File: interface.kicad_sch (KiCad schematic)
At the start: 59 parts, among them J5 5034801200, SW1 TS35CA, U10 LIS2DW12TR, U11 AP3602AKTR-G1, U8 DRV2603RUNT, U9 TPS61040DBV

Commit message: fixups before manufacturing pt1
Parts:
- removed U10: LIS2DW12TR, LIS2DW12TR:LGA-12_L2.0-W2.0-P0.50-BL, symbol LIS2DW12TR:LIS2DW12TR
- added U10: LIS3DH, Package_LGA:LGA-16_3x3mm_P0.5mm_LayoutBorder3x5y, symbol Sensor_Motion:LIS3DH
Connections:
- net ACC_3V3_IN: now also U10.1 (VDD_IO), U10.14 (VDD), U10.8 (CS)
- net GND: now also U10.10 (GND), U10.12 (GND), U10.5 (GND)
- net at JP17.1 (A): now also U10.11 (INT1)
- net at JP15.2 (B): now also U10.4 (SPC)
- net at JP14.2 (B): now also U10.6 (SDI)
- no-connect marks 8 -> 9
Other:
- moved on the sheet: C33, C34, C35, JP14, JP15, JP16, JP17

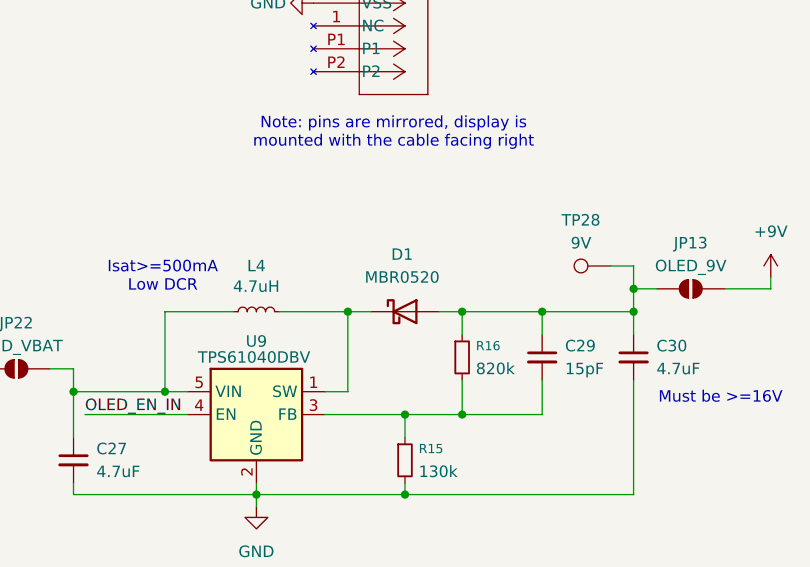
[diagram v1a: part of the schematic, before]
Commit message: oops fix: reversed diodes
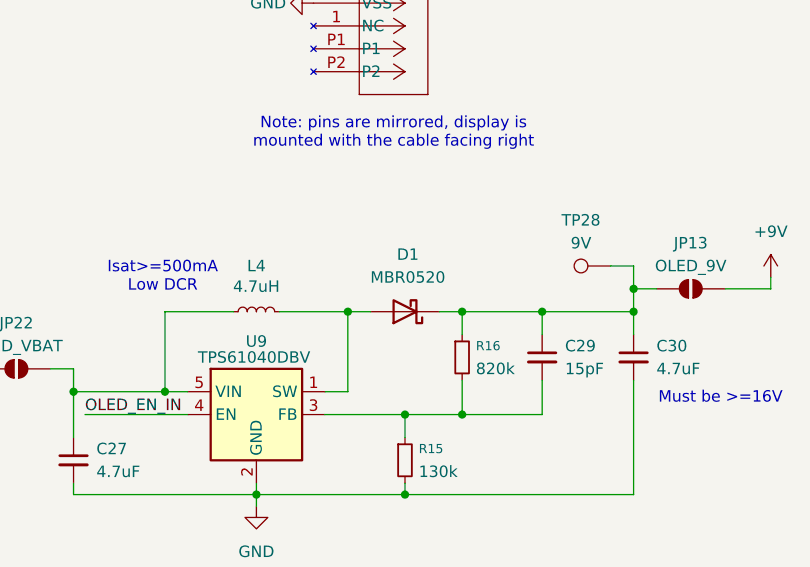
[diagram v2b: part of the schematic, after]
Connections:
- net at C29.1, C30.1, JP13.1 (A)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: now also D1.1 (K); no longer D1.2 (A)
- net at L4.2, U9.1 (SW): now also D1.2 (A); no longer D1.1 (K)
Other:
- moved on the sheet: D1
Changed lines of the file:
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@@
 	(symbol
 		(lib_id "Diode:MBR0520")
-		(at 133.35 143.51 0)
+		(at 133.35 143.51 180)
 		(unit 1)
 		(exclude_from_sim no)
@@
 		(fields_autoplaced yes)
 		(property "Reference" "D1"
-			(at 133.0325 137.16 0)
+			(at 133.6675 137.16 0)
 			(effects
 				(font
@@
 		)
 		(property "Value" "MBR0520"
-			(at 133.0325 139.7 0)
+			(at 133.6675 139.7 0)
 			(effects
 				(font
@@
 		)
 		(property "Footprint" "Diode_SMD:D_SOD-123"
-			(at 133.35 147.955 0)
+			(at 133.35 139.065 0)
 			(effects
 				(font

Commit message: oops fix: accelerometer
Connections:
- net GND: now also U10.7 (SDO)
- net at JP15.2 (B): now also U10.6 (SDI); no longer U10.4 (SPC)
- net at JP14.2 (B): now also U10.4 (SPC); no longer U10.6 (SDI)
- no-connect marks 9 -> 8
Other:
- moved on the sheet: JP14, JP15
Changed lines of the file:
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@@
 	)
 	(no_connect
-		(at 226.06 50.8)
-	)
-	(no_connect
 		(at 59.69 48.26)
 	)
@@
 	(global_label "SCL"
 		(shape input)
-		(at 194.31 48.26 180)
+		(at 194.31 55.88 180)
 		(fields_autoplaced yes)
 		(effects
@@
 		)
 		(property "Intersheetrefs" "${INTERSHEET_REFS}"
-			(at 187.8172 48.26 0)
+			(at 187.8172 55.88 0)
 			(effects
 				(font
@@
 	(global_label "SDA"
 		(shape input)
-		(at 194.31 55.88 180)
+		(at 194.31 48.26 180)
 		(fields_autoplaced yes)
 		(effects
@@
 		)
 		(property "Intersheetrefs" "${INTERSHEET_REFS}"
-			(at 187.7567 55.88 0)
+			(at 187.7567 48.26 0)
 			(effects
 				(font
@@
 	(symbol
 		(lib_id "Jumper:SolderJumper_2_Open")
-		(at 200.66 55.88 0)
+		(at 200.66 48.26 0)
 		(unit 1)
 		(exclude_from_sim no)
@@
 		(dnp no)
 		(property "Reference" "JP15"
-			(at 200.66 50.8 0)
+			(at 200.66 43.18 0)
 			(effects
 				(font
@@
 		)
 		(property "Value" "ACC_SDA"
-			(at 200.66 53.34 0)
+			(at 200.66 45.72 0)
 			(effects
 				(font
@@
 		)
 		(property "Footprint" "Jumper:SolderJumper-2_P1.3mm_Open_Pad1.0x1.5mm"
-			(at 200.66 55.88 0)
+			(at 200.66 48.26 0)
 			(effects
 				(font
@@
 		)
 		(property "Datasheet" "~"
-			(at 200.66 55.88 0)
+			(at 200.66 48.26 0)
 			(effects
 				(font
@@
 		)
 		(property "Description" "Solder Jumper, 2-pole, open"
-			(at 200.66 55.88 0)
+			(at 200.66 48.26 0)
 			(effects
 				(font
@@
 	)
 	(symbol
+		(lib_id "power:GND")
+		(at 226.06 50.8 270)
+		(unit 1)
+		(exclude_from_sim no)
+		(in_bom yes)
+		(on_board yes)
+		(dnp no)
+		(property "Reference" "#PWR013"
+			(at 219.71 50.8 0)
+			(effects
+				(font
+					(size 1.27 1.27)
+				)
+				(hide yes)
+			)
+		)
+		(property "Value" "GND"
+			(at 223.012 50.8 90)
+			(effects
+				(font
+					(size 1.27 1.27)
+				)
+				(justify right)
+			)
+		)
+		(property "Footprint" ""
+			(at 226.06 50.8 0)
+			(effects
+				(font
+					(size 1.27 1.27)
+				)
+				(hide yes)
+			)
+		)
+		(property "Datasheet" ""
+			(at 226.06 50.8 0)
+			(effects
+				(font
+					(size 1.27 1.27)
+				)
+				(hide yes)
+			)
+		)
+		(property "Description" "Power symbol creates a global label with name \"GND\" , ground"
+			(at 226.06 50.8 0)
+			(effects
+				(font
+					(size 1.27 1.27)
+				)
+				(hide yes)
+			)
+		)
+		(pin "1"
+		)
+		(instances
+			(project ""
+				(path "/c6cb5a1d-9f97-4766-8582-a9e93ed049e4/24c06676-89c1-498c-8350-9d02668ef39e"
+					(reference "#PWR013")
+					(unit 1)
+				)
+			)
+		)
+	)
+	(symbol
 		(lib_id "Device:C_Small")
 		(at 106.68 86.36 90)
@@
 	(symbol
 		(lib_id "Jumper:SolderJumper_2_Open")
-		(at 200.66 48.26 0)
+		(at 200.66 55.88 0)
 		(unit 1)
 		(exclude_from_sim no)
@@
 		(dnp no)
 		(property "Reference" "JP14"
-			(at 200.66 43.18 0)
+			(at 200.66 50.8 0)
 			(effects
 				(font
@@
 		)
 		(property "Value" "ACC_SCL"
-			(at 200.66 45.72 0)
+			(at 200.66 53.34 0)
 			(effects
 				(font
@@
 		)
 		(property "Footprint" "Jumper:SolderJumper-2_P1.3mm_Open_Pad1.0x1.5mm"
-			(at 200.66 48.26 0)
+			(at 200.66 55.88 0)
 			(effects
 				(font
@@
 		)
 		(property "Datasheet" "~"
-			(at 200.66 48.26 0)
+			(at 200.66 55.88 0)
 			(effects
 				(font
@@
 		)
 		(property "Description" "Solder Jumper, 2-pole, open"
-			(at 200.66 48.26 0)
+			(at 200.66 55.88 0)
 			(effects
 				(font

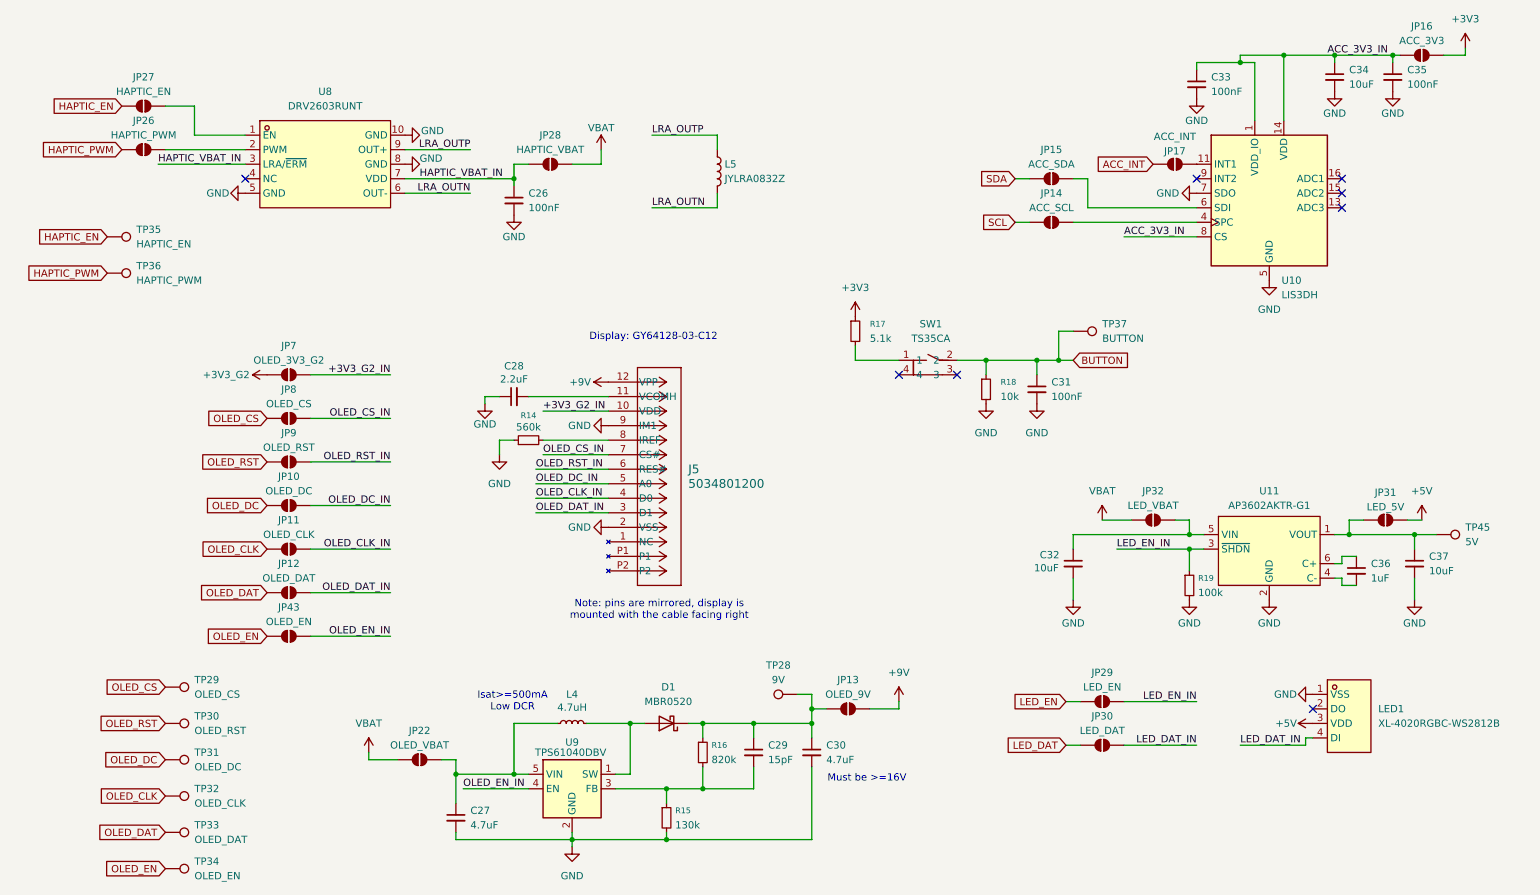
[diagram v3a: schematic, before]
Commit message: remove all jumpers
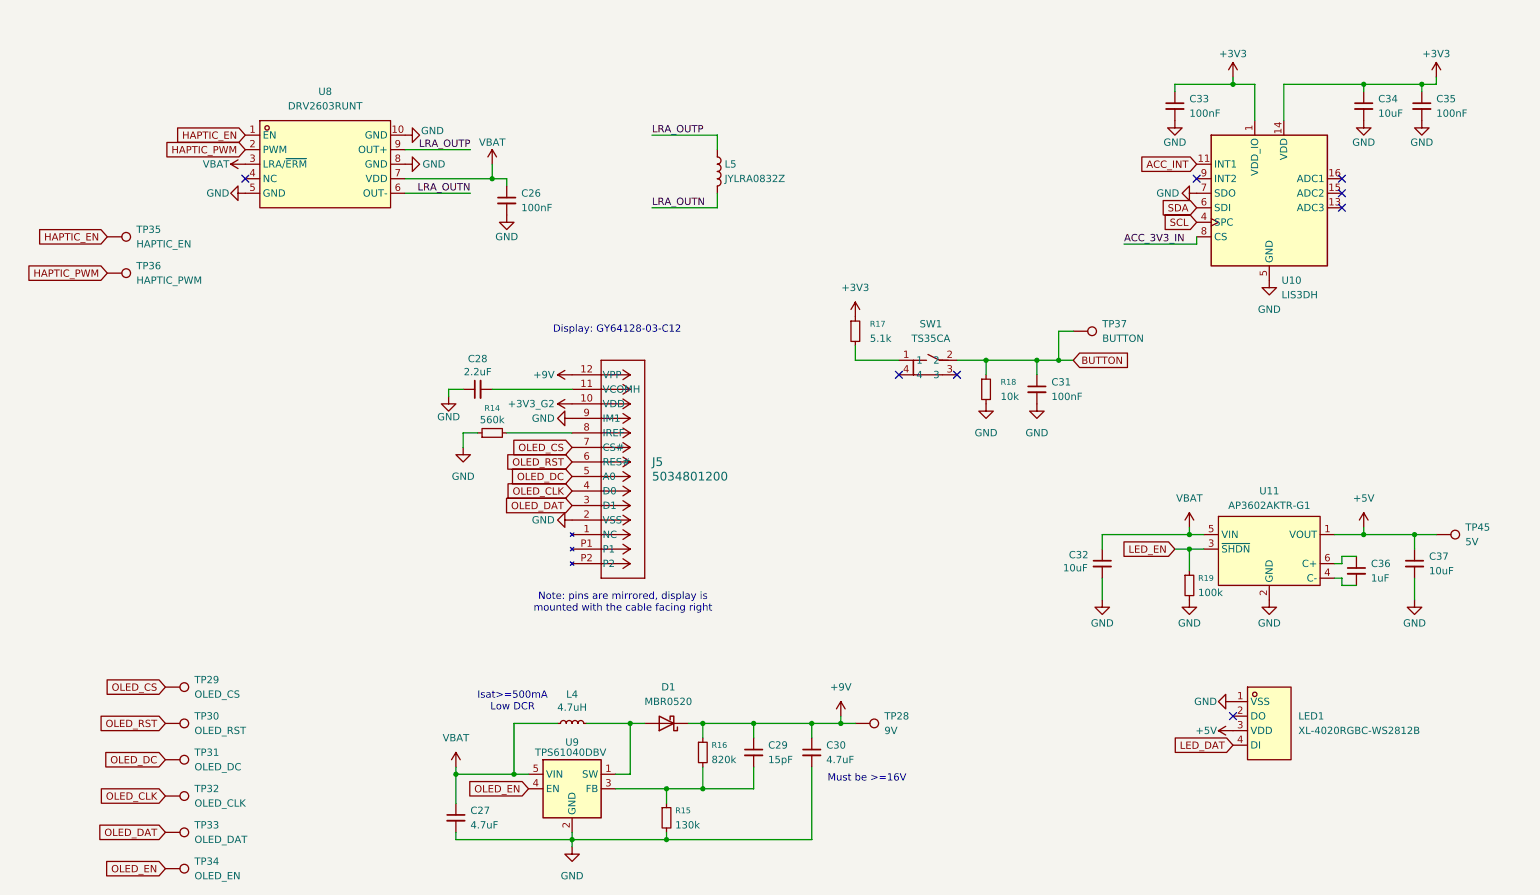
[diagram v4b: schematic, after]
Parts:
- removed JP10: OLED_DC, Jumper:SolderJumper-2_P1.3mm_Open_Pad1.0x1.5mm, symbol Jumper:SolderJumper_2_Open
- removed JP11: OLED_CLK, Jumper:SolderJumper-2_P1.3mm_Open_Pad1.0x1.5mm, symbol Jumper:SolderJumper_2_Open
- removed JP12: OLED_DAT, Jumper:SolderJumper-2_P1.3mm_Open_Pad1.0x1.5mm, symbol Jumper:SolderJumper_2_Open
- removed JP13: OLED_9V, Jumper:SolderJumper-2_P1.3mm_Open_Pad1.0x1.5mm, symbol Jumper:SolderJumper_2_Open
- removed JP14: ACC_SCL, Jumper:SolderJumper-2_P1.3mm_Open_Pad1.0x1.5mm, symbol Jumper:SolderJumper_2_Open
- removed JP15: ACC_SDA, Jumper:SolderJumper-2_P1.3mm_Open_Pad1.0x1.5mm, symbol Jumper:SolderJumper_2_Open
- removed JP16: ACC_3V3, Jumper:SolderJumper-2_P1.3mm_Open_Pad1.0x1.5mm, symbol Jumper:SolderJumper_2_Open
- removed JP17: ACC_INT, Jumper:SolderJumper-2_P1.3mm_Open_Pad1.0x1.5mm, symbol Jumper:SolderJumper_2_Open
- removed JP22: OLED_VBAT, Jumper:SolderJumper-2_P1.3mm_Open_Pad1.0x1.5mm, symbol Jumper:SolderJumper_2_Open
- removed JP26: HAPTIC_PWM, Jumper:SolderJumper-2_P1.3mm_Open_Pad1.0x1.5mm, symbol Jumper:SolderJumper_2_Open
- removed JP27: HAPTIC_EN, Jumper:SolderJumper-2_P1.3mm_Open_Pad1.0x1.5mm, symbol Jumper:SolderJumper_2_Open
- removed JP28: HAPTIC_VBAT, Jumper:SolderJumper-2_P1.3mm_Open_Pad1.0x1.5mm, symbol Jumper:SolderJumper_2_Open
- removed JP29: LED_EN, Jumper:SolderJumper-2_P1.3mm_Open_Pad1.0x1.5mm, symbol Jumper:SolderJumper_2_Open
- removed JP30: LED_DAT, Jumper:SolderJumper-2_P1.3mm_Open_Pad1.0x1.5mm, symbol Jumper:SolderJumper_2_Open
- removed JP31: LED_5V, Jumper:SolderJumper-2_P1.3mm_Open_Pad1.0x1.5mm, symbol Jumper:SolderJumper_2_Open
- removed JP32: LED_VBAT, Jumper:SolderJumper-2_P1.3mm_Open_Pad1.0x1.5mm, symbol Jumper:SolderJumper_2_Open
- removed JP43: OLED_EN, Jumper:SolderJumper-2_P1.3mm_Open_Pad1.0x1.5mm, symbol Jumper:SolderJumper_2_Open
- removed JP7: OLED_3V3_G2, Jumper:SolderJumper-2_P1.3mm_Open_Pad1.0x1.5mm, symbol Jumper:SolderJumper_2_Open
- removed JP8: OLED_CS, Jumper:SolderJumper-2_P1.3mm_Open_Pad1.0x1.5mm, symbol Jumper:SolderJumper_2_Open
- removed JP9: OLED_RST, Jumper:SolderJumper-2_P1.3mm_Open_Pad1.0x1.5mm, symbol Jumper:SolderJumper_2_Open
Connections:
- net +3V3_G2_IN is gone; now on net +3V3_G2: J5.10 (VDD)
- net HAPTIC_VBAT_IN is gone; now on net VBAT: C26.1, U8.3 (LRA/~{ERM}), U8.7 (VDD)
- net LED_DAT_IN is gone; now on net LED_DAT: LED1.4 (DI)
- net LED_EN_IN is gone; now on net LED_EN: R19.1, U11.3 (~{SHDN})
- net OLED_CLK_IN is gone; now on net OLED_CLK: J5.4 (D0)
- net OLED_CS_IN is gone; now on net OLED_CS: J5.7 (CS#)
- net OLED_DAT_IN is gone; now on net OLED_DAT: J5.3 (D1)
- net OLED_DC_IN is gone; now on net OLED_DC: J5.5 (A0)
- net OLED_EN_IN is gone; now on net OLED_EN: U9.4 (EN)
- net OLED_RST_IN is gone; now on net OLED_RST: J5.6 (RES#)
- net +3V3: now also C33.1, C34.1, C35.1, U10.1 (VDD_IO), U10.14 (VDD)
- net +5V: now also C37.1, TP45.1, U11.1 (VOUT)
- net +9V: now also C29.1, C30.1, D1.1 (K), R16.1, TP28.1
- net ACC_3V3_IN: no longer C33.1, C34.1, C35.1, U10.1 (VDD_IO), U10.14 (VDD)
- net ACC_INT: now also U10.11 (INT1)
- net HAPTIC_EN: now also U8.1 (EN)
- net HAPTIC_PWM: now also U8.2 (PWM)
- net SCL: now also U10.4 (SPC)
- net SDA: now also U10.6 (SDI)
- net VBAT: now also C27.1, C32.1, L4.1, U11.5 (VIN), U9.5 (VIN)
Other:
- moved on the sheet: C26, C28, C32, C33, C34, C35, J5, LED1, R14, TP28

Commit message: revise some decoupling caps to be 0201
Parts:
- C28: footprint Capacitor_SMD:C_0603_1608Metric -> Capacitor_SMD:C_0402_1005Metric; LCSC Part C23630 -> C12530
- C30: LCSC Part C19666 -> C1705
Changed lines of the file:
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@@
 			)
 		)
-		(property "LCSC Part" "C19666"
+		(property "LCSC Part" "C1705"
 			(at 158.75 148.59 0)
 			(effects
@@
 			)
 		)
-		(property "Footprint" "Capacitor_SMD:C_0603_1608Metric"
+		(property "Footprint" "Capacitor_SMD:C_0402_1005Metric"
 			(at 100.33 85.09 0)
 			(effects
@@
 			)
 		)
-		(property "LCSC Part" "C23630"
+		(property "LCSC Part" "C12530"
 			(at 100.33 85.09 90)
 			(effects

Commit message: layout progress
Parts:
- removed TP29: OLED_CS, TestPoint:TestPoint_Pad_D1.0mm, symbol Connector:TestPoint
- removed TP30: OLED_RST, TestPoint:TestPoint_Pad_D1.0mm, symbol Connector:TestPoint
- removed TP31: OLED_DC, TestPoint:TestPoint_Pad_D1.0mm, symbol Connector:TestPoint
- removed TP32: OLED_CLK, TestPoint:TestPoint_Pad_D1.0mm, symbol Connector:TestPoint
- removed TP33: OLED_DAT, TestPoint:TestPoint_Pad_D1.0mm, symbol Connector:TestPoint
- removed TP34: OLED_EN, TestPoint:TestPoint_Pad_D1.0mm, symbol Connector:TestPoint
- removed TP35: HAPTIC_EN, TestPoint:TestPoint_Pad_D1.0mm, symbol Connector:TestPoint
- removed TP36: HAPTIC_PWM, TestPoint:TestPoint_Pad_D1.0mm, symbol Connector:TestPoint

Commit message: progress
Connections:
- net ACC_3V3_IN is gone; now on net +3V3: U10.8 (CS)
- net +3V3_G2: now also C32.1, U11.5 (VIN)
- net VBAT: no longer C32.1, U11.5 (VIN)

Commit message: progress before minor redesign
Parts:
- removed C32, C37: 10uF, Capacitor_SMD:C_0402_1005Metric, symbol Device:C_Small
- removed C36: 1uF, Capacitor_SMD:C_0402_1005Metric, symbol Device:C_Small
- removed LED1: XL-4020RGBC-WS2812B, XL-4020RGBC-2812B:LED-SMD_4P-L4.0-W1.7_XL-4020RGBC-WS2812B, symbol XL-4020RGBC-2812B:XL-4020RGBC-WS2812B
- removed R19: 100k, Resistor_SMD:R_0402_1005Metric, symbol Device:R_Small
- removed TP45: 5V, TestPoint:TestPoint_Pad_D1.0mm, symbol Connector:TestPoint
- removed U11: AP3602AKTR-G1, AP3602AKTR-G1:SOT-23-6_L2.9-W1.6-P0.95-LS2.8-BR, symbol AP3602AKTR-G1:AP3602AKTR-G1
- added D5: KT-0805G, Diode_SMD:D_0805_2012Metric, symbol Device:LED
- added R1: 100, Resistor_SMD:R_0402_1005Metric, symbol Device:R_Small
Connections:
- net GND: now also R1.1
- net LED_DAT: now also D5.2 (A)
- new net: D5.1 (K), R1.2
- no-connect marks 8 -> 7
